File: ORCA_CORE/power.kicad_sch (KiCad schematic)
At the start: 0 parts

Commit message: persuade power board
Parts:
- added C1: 1u/50V, symbol Device:C
- added C10, C11, C12, C13, C14, C15, C18, C9: 4.7u, symbol Device:C
- added C16: 5600u, symbol Device:C_Polarized
- added C17, C3, C6, C8: 0.1u, symbol Device:C
- added C19: 10u/50V, symbol Device:C
- added C2: 0.1u25V, symbol Device:C
- added C20: 22u25V, symbol Device:C
- added C5, C7: 10u, symbol Device:C
- added D1, D2: LED_Blue, symbol Device:LED_Filled
- added D11, D9: CUHS20560, symbol Device:D_Schottky
- added D3, D4: D, symbol Device:D
- added D5: LED_Green, symbol Device:LED_Filled
- added D6, D7, D8: LED_Red, symbol Device:LED_Filled
- added F1: Fuse, symbol Device:Fuse
- added J4: Conn_01x02, symbol Connector_Generic:Conn_01x02
- added Q1: PMOS, symbol Simulation_SPICE:PMOS
- added Q2, Q3: BSS138, Package_TO_SOT_SMD:SOT-23, symbol Transistor_FET:BSS138
- added Q4: IRLML6402, Package_TO_SOT_SMD:SOT-23, symbol Transistor_FET:IRLML6402
- added R1, R15, R16, R17, R2: 10k, symbol Device:R
- added R10, R11, R12, R5, R6, R7, R8, R9: 2.2k, symbol Device:R
- added R14, R18, R20: 1k, symbol Device:R
- added R19: 10, symbol Device:R
- added R3, R4: 22k, symbol Device:R
- added U1: LTC2301IMS, symbol mylib:LTC2301IMS
- added U2: NJM78055DL1, symbol mylib:NJM7805SDL1
- added U4: G5LE149DC, symbol mylib:G5LE149DC
- added U5, U6: ~, symbol mylib:S17938DP
- added U7: NJW4860, symbol mylib:NJW4860
- added U8: AZ1117-3.3, symbol mylib:AZ1117-3.3V
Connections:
- net battery_checker: now also C3.1, Q4.2 (S), R12.1, U7.6 (INA)
- net emerg_detector: now also C17.1, R15.2, R16.1
- net emerge_order: now also U7.5 (INB)
- new net: D3.1 (K), D4.1 (K), U4.2
- new net: D4.2 (A), J4.2 (Pin_2), R14.1, R15.1, U4.5
- new net: D7.2 (A), R18.2
- new net: R3.2, R4.1, U1.5 (IN+)
- new net: C5.2, C6.2, U1.8 (REFCOMP)
- new net: D1.2 (A), R1.1
- new net: D2.2 (A), R2.2
- new net: D8.1 (K), R19.2, U6.1, U6.2, U6.3
- new net: U6.4, U7.2 (OUTA)
- new net: D6.1 (K), J4.1 (Pin_1), R18.1, U5.1, U5.2, U5.3
- new net: Q4.3 (D), R11.1, R17.2
- new net: D5.2 (A), R17.1
- new net: D8.2 (A), R20.2
- new net: D6.2 (A), R14.2
- new net: U5.4, U7.3 (OUTB)
- new net +3V3: C20.1, D11.2 (A), Q2.1 (G), Q3.1 (G), R12.2, R7.1, R9.1, U8.2 (Vout)
- new net +5V: C18.1, C19.1, C2.1, C7.1, C8.1, D11.1 (K), D9.2 (A), R10.1, R5.1, R6.1, R8.1, U1.10 (VDD), U2.2 (Vout), U7.1 (Vdd), U8.3 (Vin)
- new net +9V: C1.1, D3.2 (A), D9.1 (K), F1.2, Q4.1 (G), R11.2, R3.1, U2.3 (Vin), U4.1
- new net +BATT: Q1.1 (D), R1.2
- new net GND: C1.2, C10.2, C11.2, C12.2, C13.2, C14.2, C15.2, C16.2, C17.2, C18.2, C19.2, C2.2, C20.2, C3.2, C5.1, C6.1, C7.2, C8.2, C9.2, D1.1 (K), D2.1 (K), D5.1 (K), D7.1 (K), R16.2, R4.2, U1.1 (GND), U1.11 (AD1), U1.12 (AD0), U1.4 (GND), U1.6 (IN-), U1.9 (GDN), U2.1 (GND), U5.5, U5.6, U5.7, U5.8, U6.5, U6.6, U6.7, U6.8, U7.4 (GND), U7.7 (GND), U8.1 (GND)
- new net SCL_3V3: Q2.2 (S), R9.2
- new net SCL_5V: Q2.3 (D), R10.2, R6.2, U1.3 (SCL)
- new net SDA_3V3: Q3.2 (S), R7.2
- new net SDA_5V: Q3.3 (D), R5.2, R8.2, U1.2 (SDA)
- new net VCC: C10.1, C11.1, C12.1, C13.1, C14.1, C15.1, C16.1, C9.1, R19.1, R20.1, U4.3
- new net VDD: F1.1, Q1.2 (G), Q1.3 (S), R2.1
- no-connect marks 0 -> 3
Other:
- note added: "DCDC 5V 1.5A"
- note added: "addr 0x08"
- note added: "input output"
- note added: "relay"
- note added: "voltage feedback"

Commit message: making usp
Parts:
- added C21, C23: 1u, symbol Device:C
- added C22, C4: 4.7u, symbol Device:C
- added R13: 10k, symbol Device:R
- D1: value LED_Blue -> LED_batt
- D2: value LED_Blue -> LED_ex
- D5: value LED_Green -> LED_power
- D6: value LED_Red -> LED_emerge_switch
- D7: value LED_Red -> LED_emerge_order
- D8: value LED_Red -> LED_discharge
- R1, R2: value 10k -> 1k
- R3, R4: value 22k -> 10k
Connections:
- net +5V: no longer R10.1, R8.1
- net +BATT: now also C22.1, C23.2
- net GND: now also C21.1, C22.2, C23.1, C4.1
- net VDD: now also C21.2, C4.2, R13.2; no longer Q1.2 (G)
- net VCC renamed Vout_motor
- net battery_checker renamed power_checker
- new net: Q1.2 (G), R13.1
- new net VBUS: R10.1, R8.1
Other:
- note added: "DCDC 3V3 0.75A"
- note removed: "input output"
- moved on the sheet: C1, C19, C2, C20, D1, D11, D2, D9, F1, Q1, Q2, Q3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

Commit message: made usp (sketch only)
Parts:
- added D14: CUHS20560, symbol Device:D_Schottky
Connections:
- net +3V3: no longer Q2.1 (G), Q3.1 (G), R7.1, R9.1
- net +5V: now also R10.1, R8.1
- net VBUS: now also Q2.1 (G), Q3.1 (G), R7.1, R9.1; no longer R10.1, R8.1
- net VDD: now also D14.2 (A); no longer F1.1, Q1.3 (S)
- new net: D14.1 (K), F1.1, Q1.3 (S)
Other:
- moved on the sheet: C21, C23, C4, C5, C6, C7, C8, D2, D5, F1, Q1, R11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

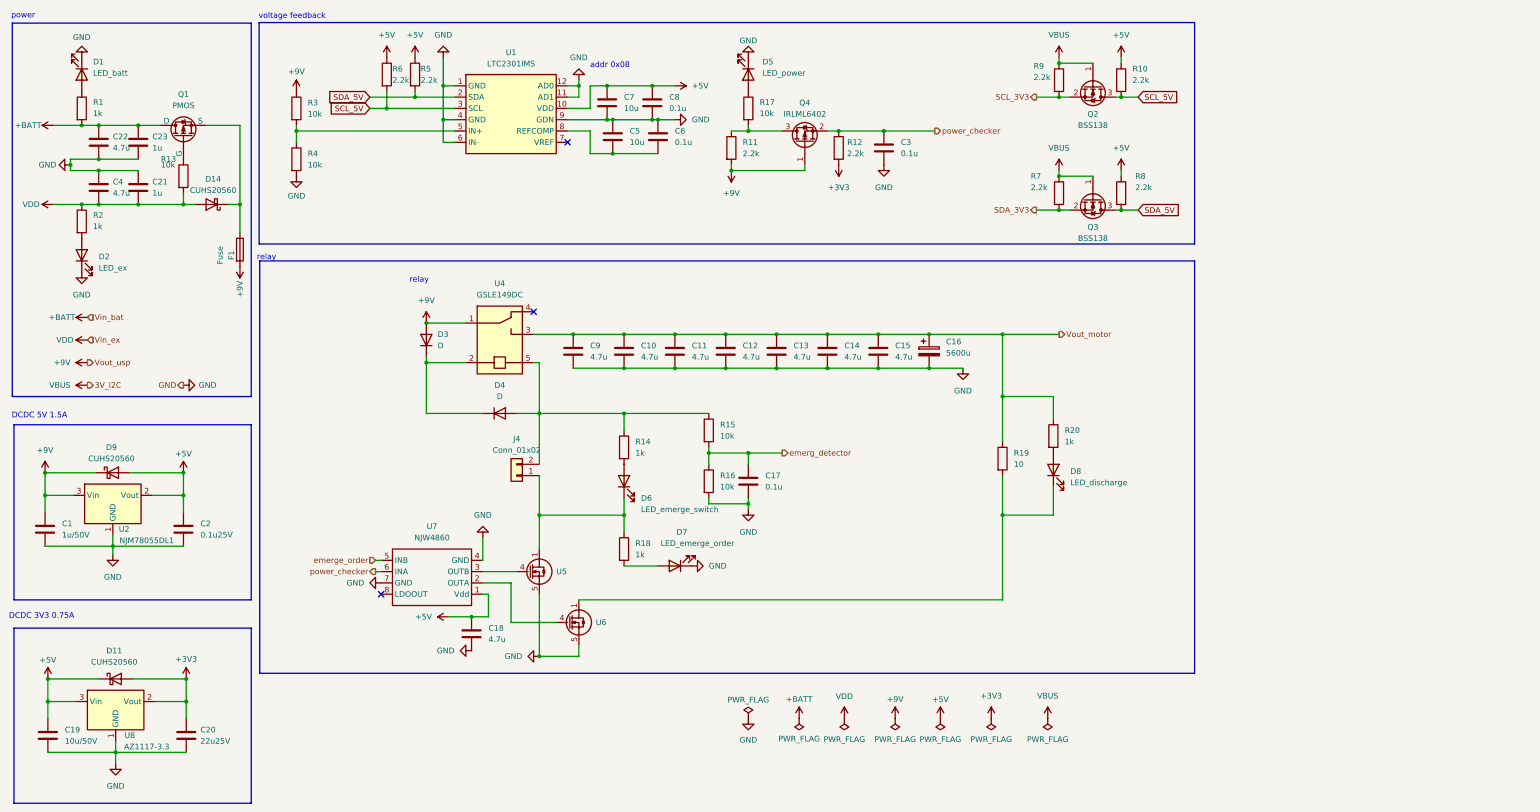
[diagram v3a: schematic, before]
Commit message: made all sketch for test (cpu board is only for test
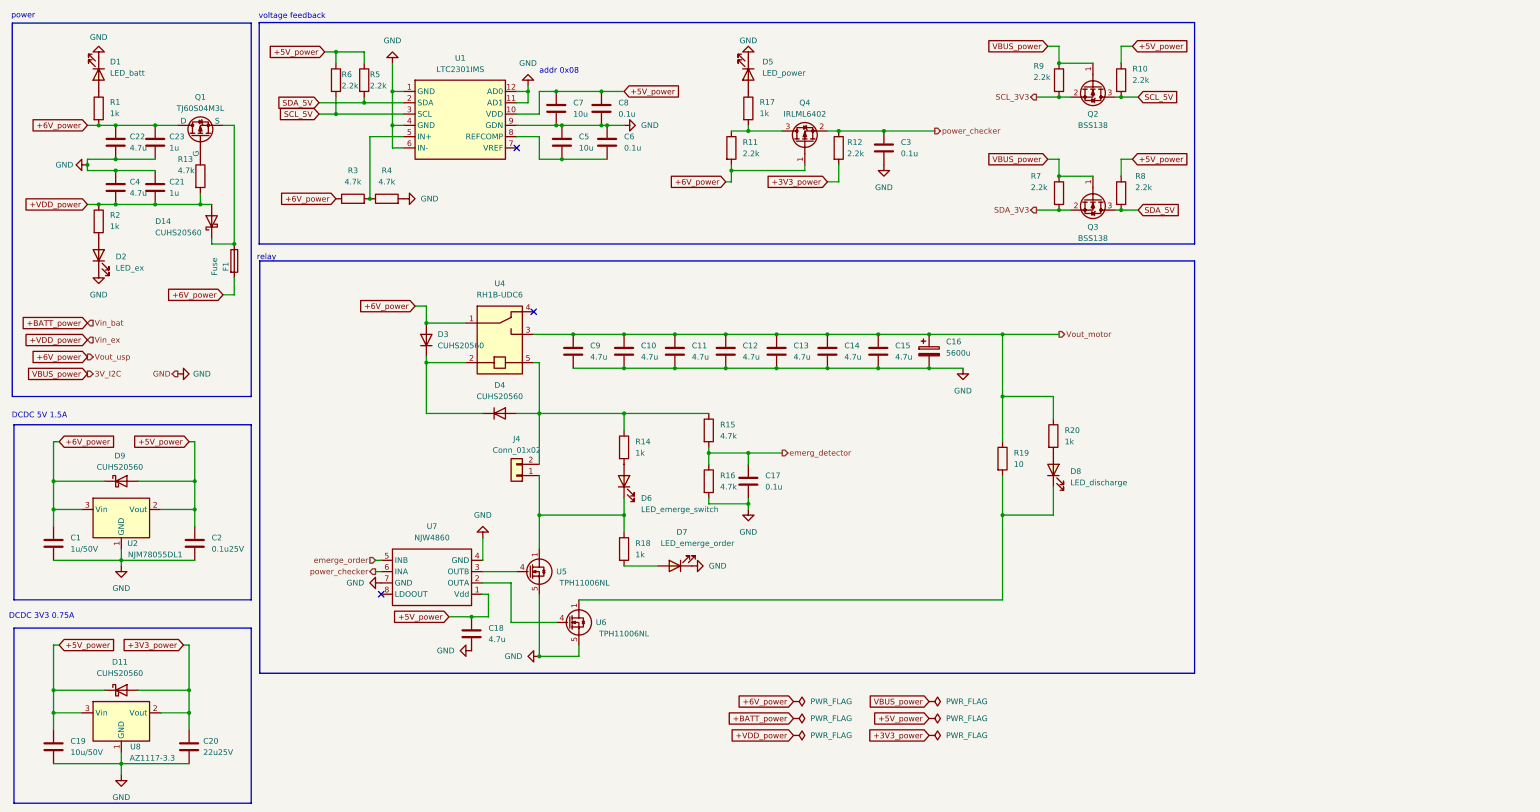
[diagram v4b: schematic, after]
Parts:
- D3, D4: value D -> CUHS20560
- Q1: value PMOS -> TJ60S04M3L
- R13, R15, R16, R3, R4: value 10k -> 4.7k
- R17: value 10k -> 1k
- U4: value G5LE149DC -> RH1B-UDC6
- U5, U6: value ~ -> TPH11006NL
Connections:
- net +BATT is gone; now on net +6V_power: C22.1, C23.2, Q1.1 (D), R1.2
- net +3V3 renamed +3V3_power
- net +5V renamed +5V_power
- net +9V renamed +6V_power
- net VBUS renamed VBUS_power
- net VDD renamed +VDD_power
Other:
- moved on the sheet: C1, C19, C2, C20, C21, C22, C23, C4, C5, C6, C7, C8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

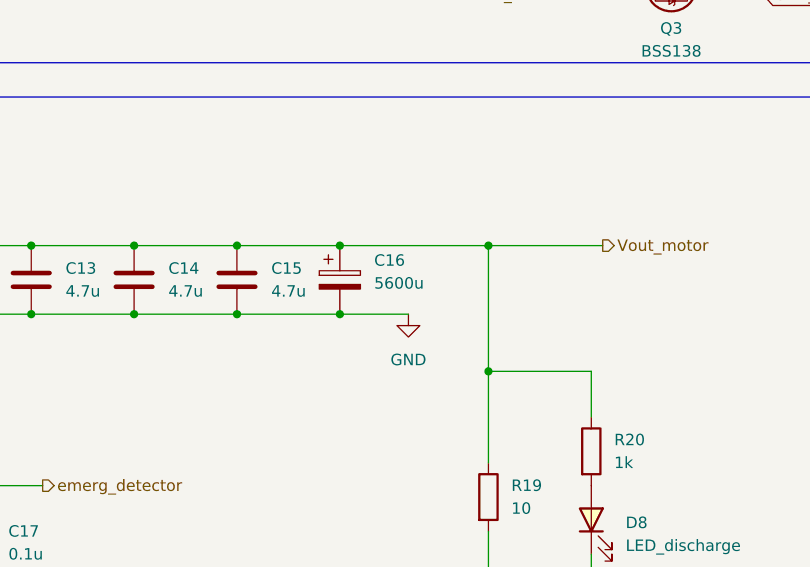
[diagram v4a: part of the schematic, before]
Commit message: attach all capacitors
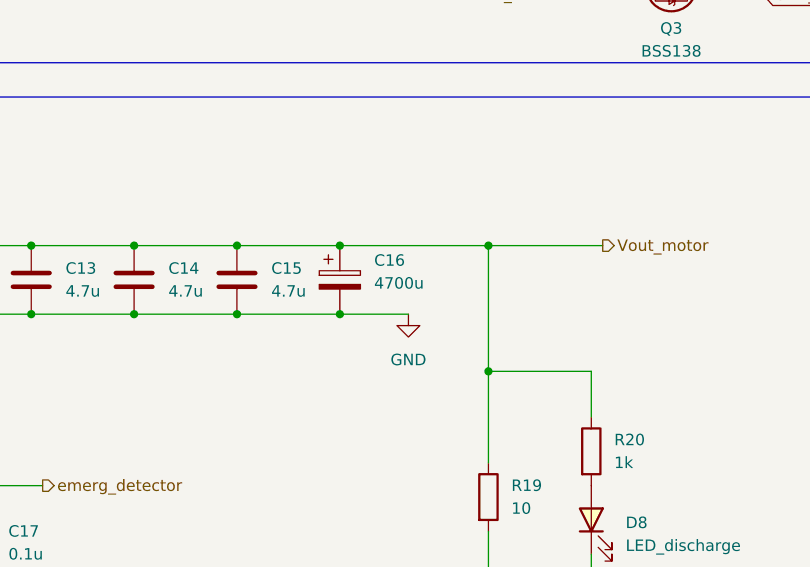
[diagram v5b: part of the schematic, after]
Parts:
- C1, C21, C23: footprint (none) -> Capacitor_SMD:C_0805_2012Metric_Pad1.18x1.45mm_HandSolder
- C10, C11, C12, C13, C14, C15, C17, C18, C2, C22, C3, C4, C6, C8, C9: footprint (none) -> Capacitor_SMD:C_0603_1608Metric_Pad1.08x0.95mm_HandSolder
- C16: value 5600u -> 4700u
- C19, C5, C7: footprint (none) -> Capacitor_SMD:C_1206_3216Metric_Pad1.33x1.80mm_HandSolder
- D1, D2, D5, D6, D7, D8: footprint (none) -> LED_SMD:LED_0603_1608Metric_Pad1.05x0.95mm_HandSolder
- D11, D14, D3, D4, D9: footprint (none) -> Diode:Diode_US2H
- Q1: footprint (none) -> toshiba:2-7M1A
- R1, R10, R11, R12, R13, R14, R15, R16, R17, R18, R19, R2, R20, R3, R4, R5, R6, R7, R8, R9: footprint (none) -> Resistor_SMD:R_0603_1608Metric_Pad0.98x0.95mm_HandSolder
- U1: footprint (none) -> Package_DFN_QFN:TDFN-12_2x3mm_P0.5mm
- U2: footprint (none) -> Package_TO_SOT_SMD:TO-252-2
- U8: footprint (none) -> Package_TO_SOT_SMD:SOT-223-3_TabPin2

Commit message: attach all the footprints
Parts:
- removed U4: RH1B-UDC6, symbol mylib:G5LE149DC
- added U4: RH1B-UDC6V, Relay_THT:RH1-U, symbol mylib:RH1B-UDC6
- C16: footprint (none) -> Capacitor_THT:CP_Radial_D16.0mm_P7.50mm
- C20: footprint (none) -> Capacitor_SMD:C_0805_2012Metric_Pad1.18x1.45mm_HandSolder
- J4: value Conn_01x02 -> emergence
- U5, U6: footprint (none) -> toshiba:2-5Q1S
- U7: footprint (none) -> nisshinbo:TSOP8-M1
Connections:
- net +6V_power: now also U4.9
- net Vout_motor: now also U4.5
- net at D3.1 (K), D4.1 (K): now also U4.14
- net at D4.2 (A), J4.2 (Pin_2), R14.1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: now also U4.13
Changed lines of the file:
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@@
   (no_connect (at 134.62 82.55))
   (no_connect (at 130.81 45.72))
+  (wire (pts (xy 251.46 128.27) (xy 251.46 121.92))
+    (stroke (width 0) (type default))
+  )
+  (wire (pts (xy 247.65 59.69) (xy 252.73 59.69))
+    (stroke (width 0) (type default))
+  )
+  (wire (pts (xy 143.51 95.25) (xy 154.94 95.25))
+    (stroke (width 0) (type default))
+  )
+  (wire (pts (xy 179.07 49.53) (xy 179.07 50.8))
+    (stroke (width 0) (type default))
+  )
+  (wire (pts (xy 179.07 50.8) (xy 195.58 50.8))
+    (stroke (width 0) (type default))
+  )
+  (wire (pts (xy 135.89 93.98) (xy 135.89 105.41))
+    (stroke (width 0) (type default))
+  )
+  (wire (pts (xy 26.67 167.64) (xy 26.67 172.72))
+    (stroke (width 0) (type default))
+  )
+  (wire (pts (xy 124.46 151.13) (xy 124.46 146.05))
+    (stroke (width 0) (type default))
+  )
+  (wire (pts (xy 55.88 157.48) (xy 57.15 157.48))
+    (stroke (width 0) (type default))
+  )
+  (wire (pts (xy 49.53 58.42) (xy 59.69 58.42))
+    (stroke (width 0) (type default))
+  )
+  (wire (pts (xy 64.77 78.74) (xy 67.31 78.74))
+    (stroke (width 0) (type default))
+  )
+  (wire (pts (xy 173.99 113.03) (xy 173.99 114.3))
+    (stroke (width 0) (type default))
+  )
+  (wire (pts (xy 252.73 34.29) (xy 255.27 34.29))
+    (stroke (width 0) (type default))
+  )
+  (wire (pts (xy 102.87 45.72) (xy 102.87 40.64))
+    (stroke (width 0) (type default))
+  )
+  (wire (pts (xy 58.42 111.76) (xy 58.42 120.65))
+    (stroke (width 0) (type default))
+  )
+  (wire (pts (xy 265.43 34.29) (xy 266.7 34.29))
+    (stroke (width 0) (type default))
+  )
+  (wire (pts (xy 182.88 41.91) (xy 190.5 41.91))
+    (stroke (width 0) (type default))
+  )
+  (wire (pts (xy 135.89 48.26) (xy 140.97 48.26))
+    (stroke (width 0) (type default))
+  )
+  (wire (pts (xy 252.73 59.69) (xy 255.27 59.69))
+    (stroke (width 0) (type default))
+  )
+  (wire (pts (xy 203.2 53.34) (xy 200.66 53.34))
+    (stroke (width 0) (type default))
+  )
+  (wire (pts (xy 173.99 114.3) (xy 173.99 116.84))
+    (stroke (width 0) (type default))
+  )
+  (wire (pts (xy 59.69 58.42) (xy 62.23 58.42))
+    (stroke (width 0) (type default))
+  )
+  (wire (pts (xy 252.73 22.86) (xy 252.73 26.67))
+    (stroke (width 0) (type default))
+  )
+  (wire (pts (xy 96.52 34.29) (xy 96.52 35.56))
+    (stroke (width 0) (type default))
+  )
   (wire (pts (xy 143.51 87.63) (xy 154.94 87.63))
-    (stroke (width 0) (type default))
-  )
-  (wire (pts (xy 251.46 128.27) (xy 251.46 121.92))
-    (stroke (width 0) (type default))
-  )
-  (wire (pts (xy 247.65 59.69) (xy 252.73 59.69))
-    (stroke (width 0) (type default))
-  )
-  (wire (pts (xy 143.51 95.25) (xy 154.94 95.25))
-    (stroke (width 0) (type default))
-  )
-  (wire (pts (xy 179.07 49.53) (xy 179.07 50.8))
-    (stroke (width 0) (type default))
-  )
-  (wire (pts (xy 179.07 50.8) (xy 195.58 50.8))
-    (stroke (width 0) (type default))
-  )
-  (wire (pts (xy 135.89 93.98) (xy 135.89 105.41))
-    (stroke (width 0) (type default))
-  )
-  (wire (pts (xy 26.67 167.64) (xy 26.67 172.72))
-    (stroke (width 0) (type default))
-  )
-  (wire (pts (xy 124.46 151.13) (xy 124.46 146.05))
-    (stroke (width 0) (type default))
-  )
-  (wire (pts (xy 55.88 157.48) (xy 57.15 157.48))
-    (stroke (width 0) (type default))
-  )
-  (wire (pts (xy 49.53 58.42) (xy 59.69 58.42))
-    (stroke (width 0) (type default))
-  )
-  (wire (pts (xy 64.77 78.74) (xy 67.31 78.74))
-    (stroke (width 0) (type default))
-  )
-  (wire (pts (xy 173.99 113.03) (xy 173.99 114.3))
-    (stroke (width 0) (type default))
-  )
-  (wire (pts (xy 252.73 34.29) (xy 255.27 34.29))
-    (stroke (width 0) (type default))
-  )
-  (wire (pts (xy 102.87 45.72) (xy 102.87 40.64))
-    (stroke (width 0) (type default))
-  )
-  (wire (pts (xy 58.42 111.76) (xy 58.42 120.65))
-    (stroke (width 0) (type default))
-  )
-  (wire (pts (xy 265.43 34.29) (xy 266.7 34.29))
-    (stroke (width 0) (type default))
-  )
-  (wire (pts (xy 182.88 41.91) (xy 190.5 41.91))
-    (stroke (width 0) (type default))
-  )
-  (wire (pts (xy 135.89 48.26) (xy 140.97 48.26))
-    (stroke (width 0) (type default))
-  )
-  (wire (pts (xy 252.73 59.69) (xy 255.27 59.69))
-    (stroke (width 0) (type default))
-  )
-  (wire (pts (xy 203.2 53.34) (xy 200.66 53.34))
-    (stroke (width 0) (type default))
-  )
-  (wire (pts (xy 173.99 114.3) (xy 173.99 116.84))
-    (stroke (width 0) (type default))
-  )
-  (wire (pts (xy 59.69 58.42) (xy 62.23 58.42))
-    (stroke (width 0) (type default))
-  )
-  (wire (pts (xy 252.73 22.86) (xy 252.73 26.67))
-    (stroke (width 0) (type default))
-  )
-  (wire (pts (xy 96.52 34.29) (xy 96.52 35.56))
     (stroke (width 0) (type default))
   )
@@
     )
   )
-  (symbol (lib_id "mylib:G5LE149DC") (at 127 90.17 0) (unit 1)
-    (in_bom yes) (on_board yes) (dnp no)
-    (property "Reference" "U4" (at 127 76.2 0)
-      (effects (font (size 1.27 1.27)))
-    )
-    (property "Value" "RH1B-UDC6" (at 127 78.74 0)
-      (effects (font (size 1.27 1.27)))
-    )
-    (property "Footprint" "" (at 127 90.17 0)
-      (effects (font (size 1.27 1.27)) hide)
-    )
-    (property "Datasheet" "" (at 127 90.17 0)
-      (effects (font (size 1.27 1.27)) hide)
-    )
-    (pin "3")
-    (pin "2")
-    (pin "5")
-    (pin "4")
-    (pin "1")
-    (instances
-      (project "ORCA_CORE"
-        (path "/895d6bb7-4008-488b-a34b-0077e9f7e4a1/62c40b6d-2f8c-4265-a550-d6ec27759bcd"
-          (reference "U4") (unit 1)
-        )
-      )
-    )
-  )
   (symbol (lib_id "Device:C") (at 213.36 45.72 0) (unit 1)
     (in_bom yes) (on_board yes) (dnp no) (fields_autoplaced)
@@
   )
   (symbol (lib_id "Device:D") (at 110.49 88.9 90) (unit 1)
-    (in_bom yes) (on_board yes) (dnp no) (fields_autoplaced)
-    (property "Reference" "D3" (at 113.03 87.63 90)
+    (in_bom yes) (on_board yes) (dnp no)
+    (property "Reference" "D3" (at 96.52 87.63 90)
       (effects (font (size 1.27 1.27)) (justify right))
     )
-    (property "Value" "CUHS20560" (at 113.03 90.17 90)
+    (property "Value" "CUHS20560" (at 96.52 90.17 90)
       (effects (font (size 1.27 1.27)) (justify right))
     )
@@
       (effects (font (size 1.27 1.27)) (justify left))
     )
-    (property "Footprint" "" (at 58.1152 184.15 0)
+    (property "Footprint" "Capacitor_SMD:C_0805_2012Metric_Pad1.18x1.45mm_HandSolder" (at 58.1152 184.15 0)
       (effects (font (size 1.27 1.27)) hide)
     )
@@
       (effects (font (size 1.27 1.27)))
     )
-    (property "Footprint" "" (at 144.78 152.4 0)
+    (property "Footprint" "toshiba:2-5Q1S" (at 144.78 152.4 0)
       (effects (font (size 1.27 1.27)) hide)
     )
@@
     )
   )
+  (symbol (lib_id "mylib:RH1B-UDC6") (at 127 90.17 0) (unit 1)
+    (in_bom yes) (on_board yes) (dnp no)
+    (property "Reference" "U4" (at 127 77.47 0)
+      (effects (font (size 1.27 1.27)))
+    )
+    (property "Value" "RH1B-UDC6V" (at 127 80.01 0)
+      (effects (font (size 1.27 1.27)))
+    )
+    (property "Footprint" "Relay_THT:RH1-U" (at 127 90.17 0)
+      (effects (font (size 1.27 1.27)) hide)
+    )
+    (property "Datasheet" "" (at 127 90.17 0)
+      (effects (font (size 1.27 1.27)) hide)
+    )
+    (pin "9")
+    (pin "1")
+    (pin "14")
+    (pin "13")
+    (pin "5")
+    (instances
+      (project "ORCA_CORE"
+        (path "/895d6bb7-4008-488b-a34b-0077e9f7e4a1/62c40b6d-2f8c-4265-a550-d6ec27759bcd"
+          (reference "U4") (unit 1)
+        )
+      )
+    )
+  )
   (symbol (lib_id "Device:C") (at 120.65 154.94 0) (unit 1)
     (in_bom yes) (on_board yes) (dnp no) (fields_autoplaced)
@@
       (effects (font (size 1.27 1.27)))
     )
-    (property "Value" "Conn_01x02" (at 130.81 113.665 0)
+    (property "Value" "emergence" (at 130.81 113.665 0)
       (effects (font (size 1.27 1.27)))
     )
@@
       (effects (font (size 1.27 1.27)))
     )
-    (property "Footprint" "" (at 111.76 142.24 0)
+    (property "Footprint" "nisshinbo:TSOP8-M1" (at 111.76 142.24 0)
       (effects (font (size 1.27 1.27)) hide)
     )
@@
       (effects (font (size 1.27 1.27)))
     )
-    (property "Footprint" "" (at 135.89 140.97 0)
+    (property "Footprint" "toshiba:2-5Q1S" (at 135.89 140.97 0)
       (effects (font (size 1.27 1.27)) hide)
     )
@@
       (effects (font (size 1.27 1.27)) (justify left))
     )
-    (property "Footprint" "" (at 224.4852 95.25 0)
-      (effects (font (size 1.27 1.27)) hide)
-    )
+    (property "Footprint" "Capacitor_THT:CP_Radial_D16.0mm_P7.50mm" (at 224.4852 95.25 0)
+      (effects (font (size 1.27 1.27)) hide)
+    )

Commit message: change sketch a little
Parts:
- F1: footprint (none) -> fuse:fuse
- J4: footprint (none) -> Connector_JST:JST_XH_B2B-XH-A_1x02_P2.50mm_Vertical
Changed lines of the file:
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@@
       (effects (font (size 1.27 1.27)))
     )
-    (property "Footprint" "" (at 65.532 71.12 90)
+    (property "Footprint" "fuse:fuse" (at 65.532 71.12 90)
       (effects (font (size 1.27 1.27)) hide)
     )
@@
       (effects (font (size 1.27 1.27)))
     )
-    (property "Footprint" "" (at 130.81 119.38 0)
-      (effects (font (size 1.27 1.27)) hide)
-    )
+    (property "Footprint" "Connector_JST:JST_XH_B2B-XH-A_1x02_P2.50mm_Vertical" (at 130.81 119.38 0)
+      (effects (font (size 1.27 1.27)) hide)
+    )
